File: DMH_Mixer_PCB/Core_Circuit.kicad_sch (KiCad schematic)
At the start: 38 parts, among them SW1 SW_SPDT_321, SW2 SW_SPDT_321, SW3 SW_SPDT_321, SW4 SW_SPDT_321, U1 TL074

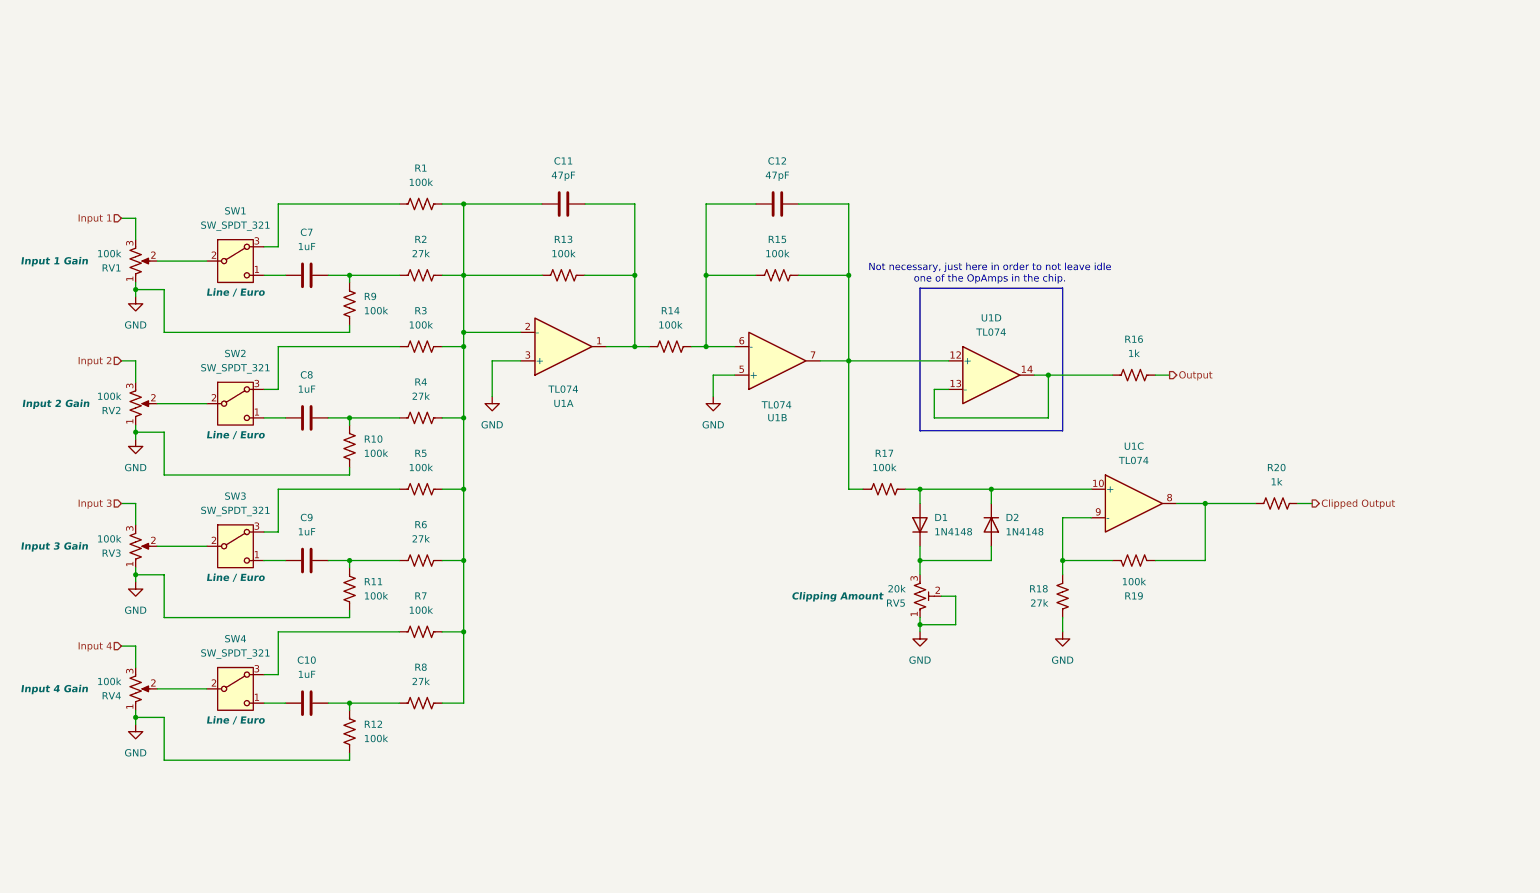
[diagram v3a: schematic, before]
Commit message: Added Zener limiting
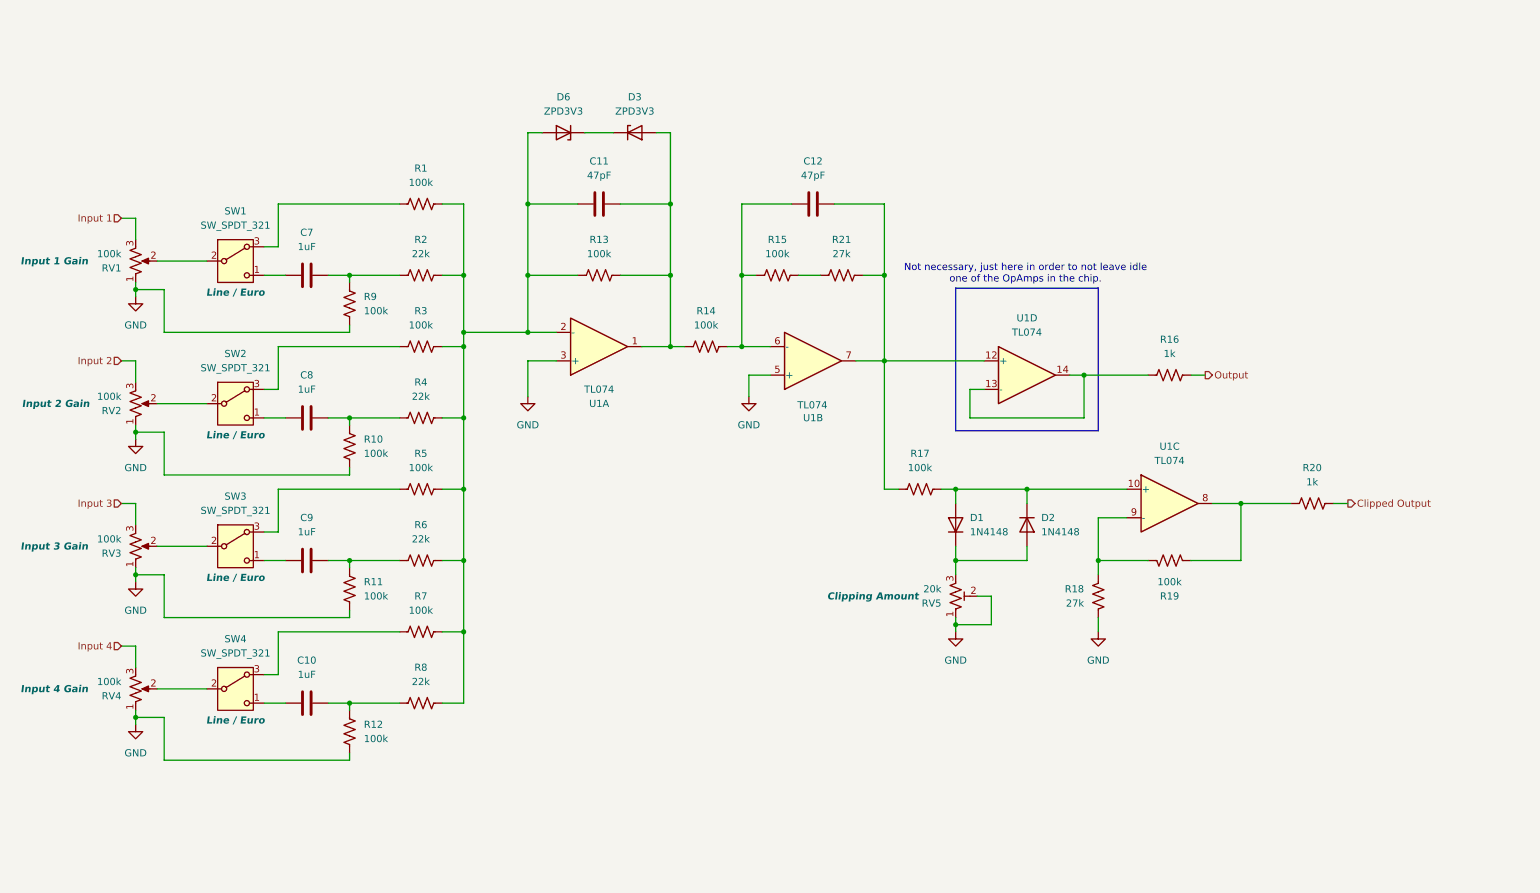
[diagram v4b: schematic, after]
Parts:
- added D3, D6: ZPD3V3, Diode_THT:D_DO-35_SOD27_P7.62mm_Horizontal, symbol Device:D_Zener
- added R21: 27k, Resistor_THT:R_Axial_DIN0207_L6.3mm_D2.5mm_P7.62mm_Horizontal, symbol Device:R_US
- R2, R4, R6, R8: value 27k -> 22k
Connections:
- net at C11.1, R1.2, R13.1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: now also D6.2 (A)
- net at C12.2, R17.1, U1.12 (+)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: now also R21.2; no longer R15.2
- net at C11.2, R13.2, R14.1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: now also D3.2 (A)
- new net: D3.1 (K), D6.1 (K)
- new net: R15.2, R21.1
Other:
- moved on the sheet: C11, C12, D1, D2, R13, R14, R16, R17, R18, R19, R20, RV5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

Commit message: Update Core_Circuit.kicad_sch
Added 47pF to last opamp stage
Changed zeners to 3V9
Changed additional gain resistor to 100k
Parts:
- added C13: 47pF, Capacitor_THT:C_Disc_D3.0mm_W2.0mm_P2.50mm, symbol Device:C
- D3, D6: value ZPD3V3 -> ZPD3V9
- R21: value 27k -> 100k
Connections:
- net at R19.2, R20.1, U1.8: now also C13.2
- net at R18.2, R19.1, U1.9 (-): now also C13.1
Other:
- moved on the sheet: D1, D2, R17, R18, R19, R20, RV5, U1C

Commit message: Output selection in progress
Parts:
- added SW5: SW_DPDT, SynthStuff:PinHeader_2x03_P2.54mm_Vertical_142536, symbol SynthStuff:Switch_3PDT
- added SW6, SW7, SW8, SW9: SW_SPDT_MSM, symbol Switch:SW_SPDT_MSM
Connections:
- net at C13.2, R19.2, U1.8: now also SW9.3 (4); no longer R20.1
- net at C12.2, R17.1, U1.7: now also R15.2; no longer R21.2, U1.12 (+)
- net at D3.1 (K): now also SW7.1; no longer D6.1 (K)
- net at C11.2, D3.2 (A), R13.2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: now also R21.2
- net at R21.1: now also SW6.2 (3); no longer R15.2
- net at C12.1, R14.2, R15.1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: now also SW6.1
- new net: SW8.2 (3), U1.12 (+)
- new net: D6.1 (K), SW7.2 (3)
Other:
- note removed: "Not necessary, just here in order to not leave idle one of the OpAmps in the chip."
- moved on the sheet: C10, C11, C12, C13, C7, C8, C9, D1, D2, D3, D6, R1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

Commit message: Finalization in progress
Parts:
- removed C13: 47pF, Capacitor_THT:C_Disc_D3.0mm_W2.0mm_P2.50mm, symbol Device:C
- removed D1, D2: 1N4148, Diode_THT:D_DO-35_SOD27_P7.62mm_Horizontal, symbol Device:D
- removed R17, R19: 100k, Resistor_THT:R_Axial_DIN0207_L6.3mm_D2.5mm_P7.62mm_Horizontal, symbol Device:R_US
- removed R18: 27k, Resistor_THT:R_Axial_DIN0207_L6.3mm_D2.5mm_P7.62mm_Horizontal, symbol Device:R_US
- removed R20: 1k, Resistor_THT:R_Axial_DIN0207_L6.3mm_D2.5mm_P7.62mm_Horizontal, symbol Device:R_US
- removed RV5: 20k, Potentiometer_THT:Potentiometer_Bourns_3296W_Vertical, symbol Device:R_Potentiometer_Trim_US
- removed SW5: SW_DPDT, SynthStuff:PinHeader_2x03_P2.54mm_Vertical_142536, symbol SynthStuff:Switch_3PDT
- removed SW6, SW7, SW8, SW9: SW_SPDT_MSM, symbol Switch:SW_SPDT_MSM
- removed unit 3 of U1
- removed unit 4 of U1
- added SW5: SW_DPDT, SynthStuff:PinHeader_2x03_P2.54mm_Vertical_142536, symbol SynthStuff:Switch_DPDT_On_Off_On
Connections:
- net at C12.2, R15.2, U1.7: now also R16.1
- net at C12.1, R14.2, R15.1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: now also SW5.4 (A)
- net at R21.1: now also SW5.5 (B)
- net at D3.1 (K): now also SW5.2 (B)
- net at D6.1 (K): now also SW5.1 (A)
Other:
- moved on the sheet: R16

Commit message: Finalized schematic
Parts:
- removed R10, R11, R12, R9: 100k, Resistor_THT:R_Axial_DIN0207_L6.3mm_D2.5mm_P7.62mm_Horizontal, symbol Device:R_US
- removed U1: TL074, Package_DIP:DIP-14_W7.62mm_Socket, symbol Amplifier_Operational:TL074
- added U1: TL072, Package_DIP:DIP-8_W7.62mm_Socket, symbol Amplifier_Operational:TL072
- SW5: symbol SynthStuff:Switch_DPDT_On_Off_On -> SynthStuff:Switch_DPDT
- renumbered D6 to D3, D3 to D4, R14 to R10, R21 to R11, R15 to R12, R16 to R13, R13 to R9
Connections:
- net GND: now also U1.3 (+), U1.5 (+)
- net at C11.1, D3.2 (A), R1.2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: now also U1.2 (-)
- net at C12.1, R10.2, R12.1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: now also U1.6 (-)
- net at C11.2, D4.2 (A), R10.1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: now also U1.1
- net at C12.2, R12.2, R13.1: now also U1.7
- no-connect marks 0 -> 2
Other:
- note added: "Euro"
- note added: "Line"
